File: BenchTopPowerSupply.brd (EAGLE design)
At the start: 160 x 100 mm, 129 parts, among them U10 E2A-T220-25E, U7 STM32F103C8T6, U8 E2A-T220-25E, U9 E2A-T220-25E, X1 5566-24, Y1 8MHZ

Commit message: Fixing schematic issues
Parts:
- added R34: 1M, rcl:R1206
- moved LED1 11.9 mm to (98.7, 35.7)
- moved C19 6.51 mm to (112.4, 26.5), flipped to the top, turned to 225 degrees
- moved R23 2.51 mm to (105.4, 39.1), turned to 0 degrees
- moved C18 1.13 mm to (107.4, 31.9), turned to 225 degrees
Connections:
- new net N$10: C18.2, C19.2
- net BOOT1: now also U7.20; no longer U7.19
- net GND: no longer C18.2, C19.2
- net N$3: now also R34.2
- net N$5: now also R34.1
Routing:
- net N$10: track 0.00 -> 9.96 mm
- net N$3: track 11.2 -> 16.6 mm
- net N$5: track 15.5 -> 17.9 mm
- net N$28: track 7.26 -> 6.16 mm
- net N$27: track 7.04 -> 7.60 mm

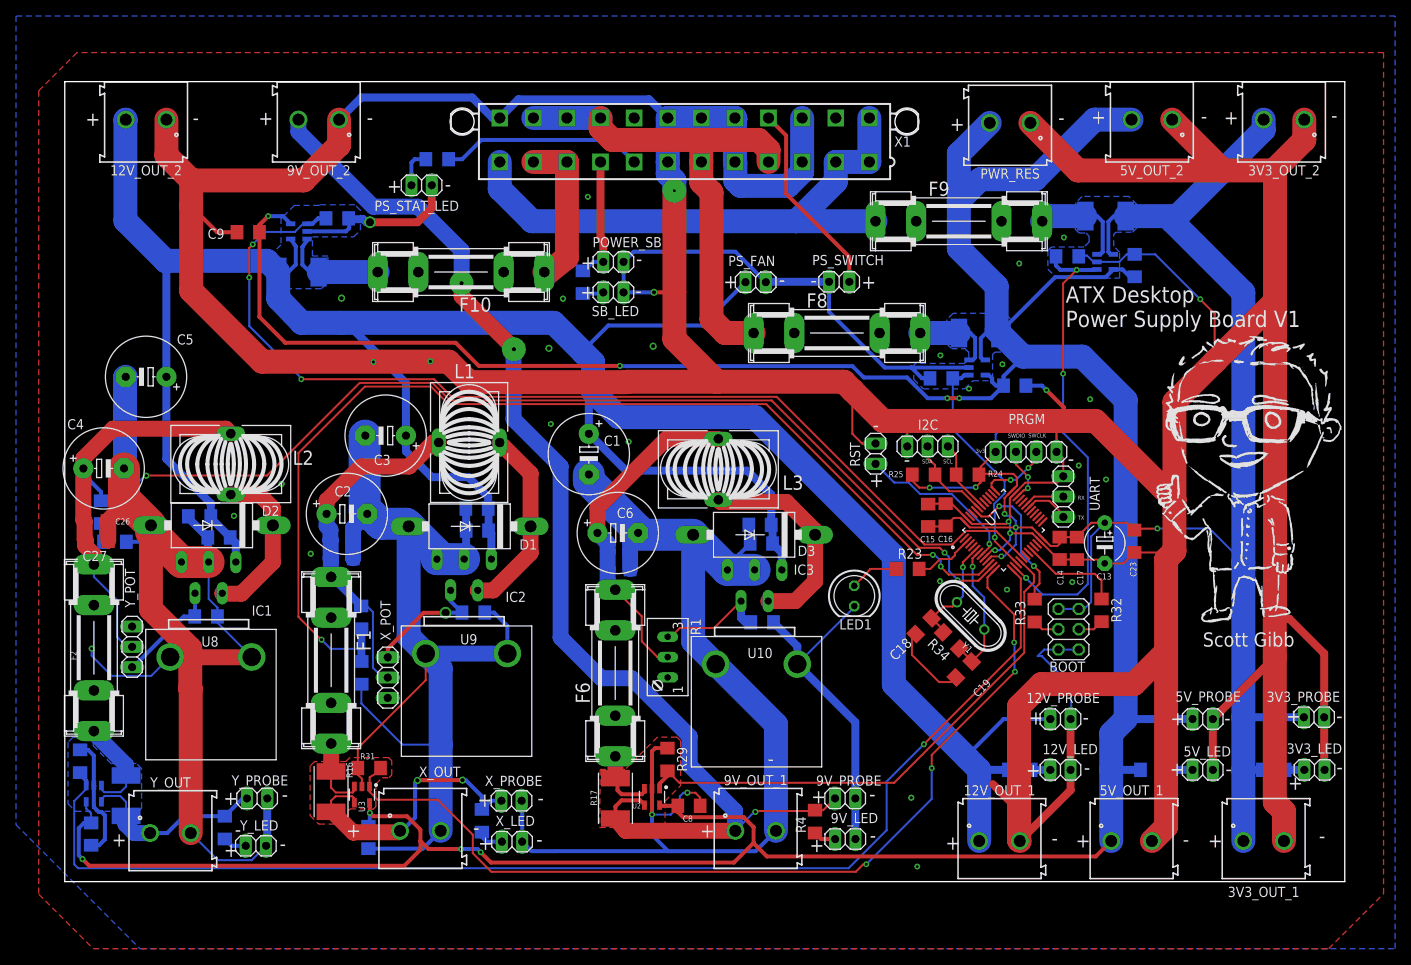
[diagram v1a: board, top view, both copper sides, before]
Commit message: Adding mounting holes to the design and experimenting with JLCPCB SMT assembly
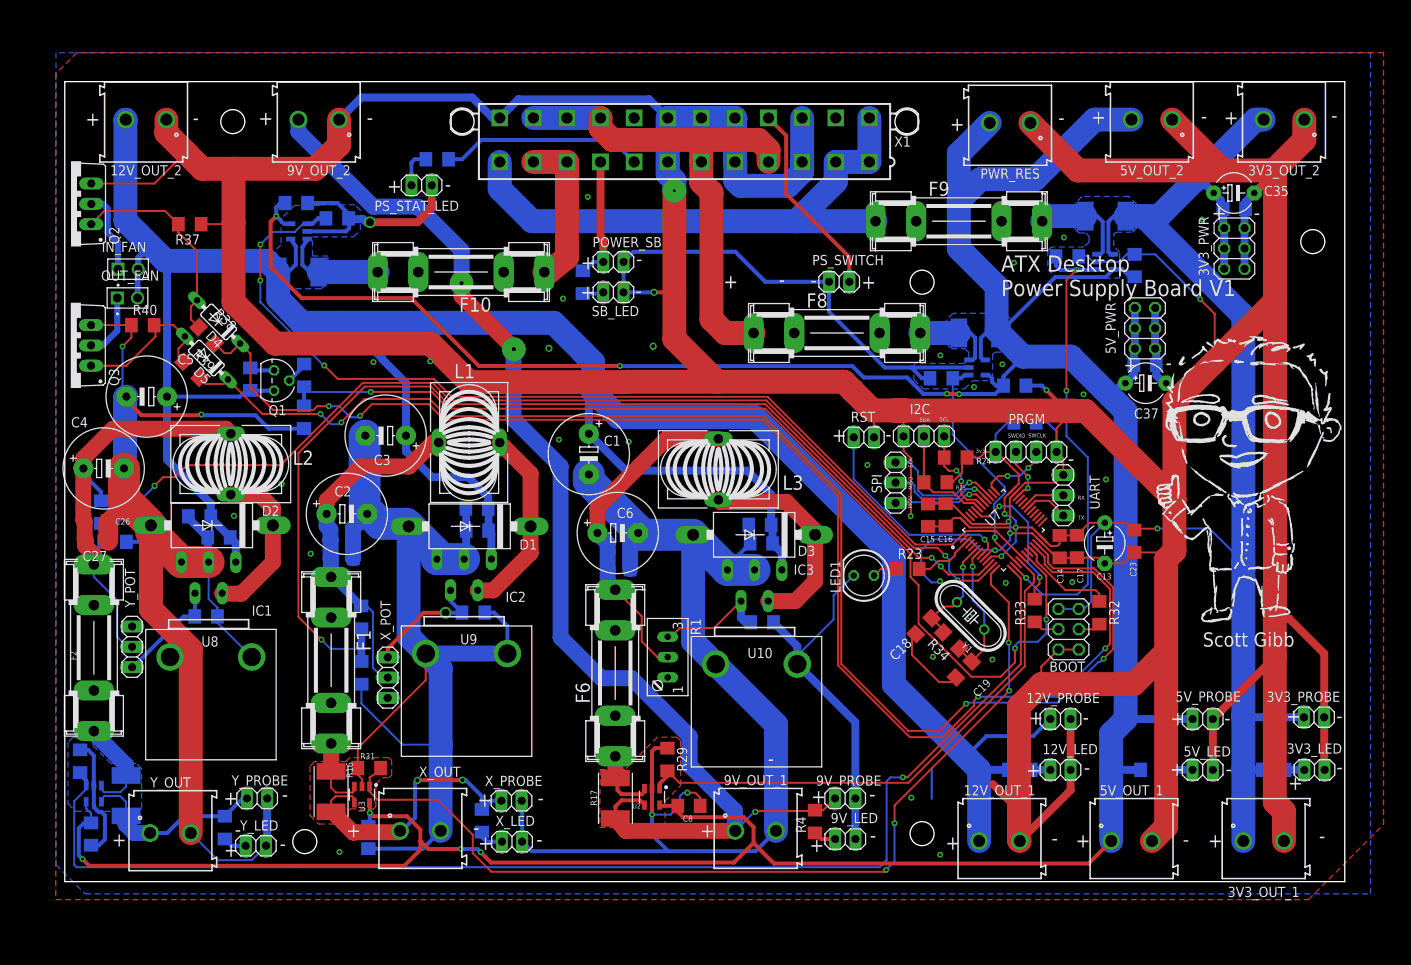
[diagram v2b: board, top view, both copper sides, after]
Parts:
- removed PS_FAN: (no value), pinhead:1X02
- added 3V3_PWR, 5V_PWR: PINHD-2X3, Connector:2X03
- added C34: 100nF, rcl:C1206
- added C35, C37: 100nF, rcl:E5-5
- added C36, C38: 100uF, rcl:C1206
- added D4, D5: 1N4148DO35-7, diode:DO35-7
- added IN_FAN, OUT_FAN: 61300211121, Headers:61300211121
- added Q1: NPN, Transistor:TO92
- added Q2, Q3: IRF510, transistor-power:TO220BV
- added R35, R36, R37, R40: 10k, rcl:R1206
- added R38, R39: 470, rcl:R1206
- added SPI: PINHD-1X3, Connector:1X03
- R1: value (none) -> 100k
- moved C9 7.03 mm to (28.9, 84.8), flipped to the bottom
- moved LED1 2.82 mm to (99.9, 38.3), turned to 180 degrees
- moved R24 2.61 mm to (111.4, 53.0)
- moved RST 2.51 mm to (99.9, 55.5), turned to 180 degrees
- moved C5 2.48 mm to (10.2, 60.6)
- moved R25 1.76 mm to (108.8, 49.9), turned to 0 degrees
- moved I2C 1.34 mm to (107.4, 55.7)
- moved R32 0.41 mm to (129.3, 33.6)
- moved C17 0.24 mm to (126.5, 41.9)
- moved C14 0.20 mm to (124.4, 41.9)
- moved UART 0.17 mm to (124.8, 48.3)
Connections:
- new net IN_FAN_PWM: D4.C, R38.2, U7.21
- new net N$26: Q1.2, R35.2
- new net N$30: D4.A, Q2.G, R37.2, R38.1
- new net N$31: IN_FAN.1, Q2.D
- new net N$32: D5.A, Q3.G, R39.1, R40.2
- new net N$35: OUT_FAN.1, Q3.D
- new net OUT_FAN_PWM: D5.C, R39.2, U7.22
- new net SPI_MISO: SPI.2, U7.40
- new net SPI_MOSI: SPI.3, U7.41
- new net SPI_NSS: U7.38
- new net SPI_SCK: SPI.1, U7.39
- new net TEMP_SENS: R35.1, R36.2, U7.18
- net +12V: now also C34.1, IN_FAN.2, OUT_FAN.2, Q1.1; no longer PS_FAN.1
- net +3V3: now also 3V3_PWR.1, 3V3_PWR.3, 3V3_PWR.5, C35.+, C36.2
- net +5V: now also 5V_PWR.1, 5V_PWR.3, 5V_PWR.5, C37.+, C38.2
- net GND: now also 3V3_PWR.2, 3V3_PWR.4, 3V3_PWR.6, 5V_PWR.2, 5V_PWR.4, 5V_PWR.6, C34.2, C35.-, C36.1, C37.-, C38.1, Q1.3, Q2.S, Q3.S, R36.1, R37.1, R40.1; no longer PS_FAN.2
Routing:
- net IN_FAN_PWM: track 0.00 -> 174.2 mm, vias 0 -> 4
- net OUT_FAN_PWM: track 0.00 -> 172.4 mm, vias 0 -> 4
- net TEMP_SENS: track 0.00 -> 130.2 mm, vias 0 -> 3
- net GND: track 1310.7 -> 1391.4 mm, vias 36 -> 42
- net N$30: track 0.00 -> 26.8 mm
- net N$32: track 0.00 -> 19.8 mm
- net SPI_SCK: track 0.00 -> 16.3 mm, vias 0 -> 1
- net SPI_MISO: track 0.00 -> 13.8 mm, vias 0 -> 1
- net SPI_MOSI: track 0.00 -> 11.9 mm, vias 0 -> 1
- net N$31: track 0.00 -> 10.4 mm
- net +3V3: track 221.2 -> 231.2 mm, vias 6 -> 4
- net +5V: track 461.2 -> 469.4 mm
- net N$35: track 0.00 -> 8.14 mm
- net N$25: track 21.1 -> 27.2 mm
- net X_CURR_OUT: track 118.1 -> 122.9 mm
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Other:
- board text added: "MISO"
- board text added: "MOSI"
- board text added: "SCK"

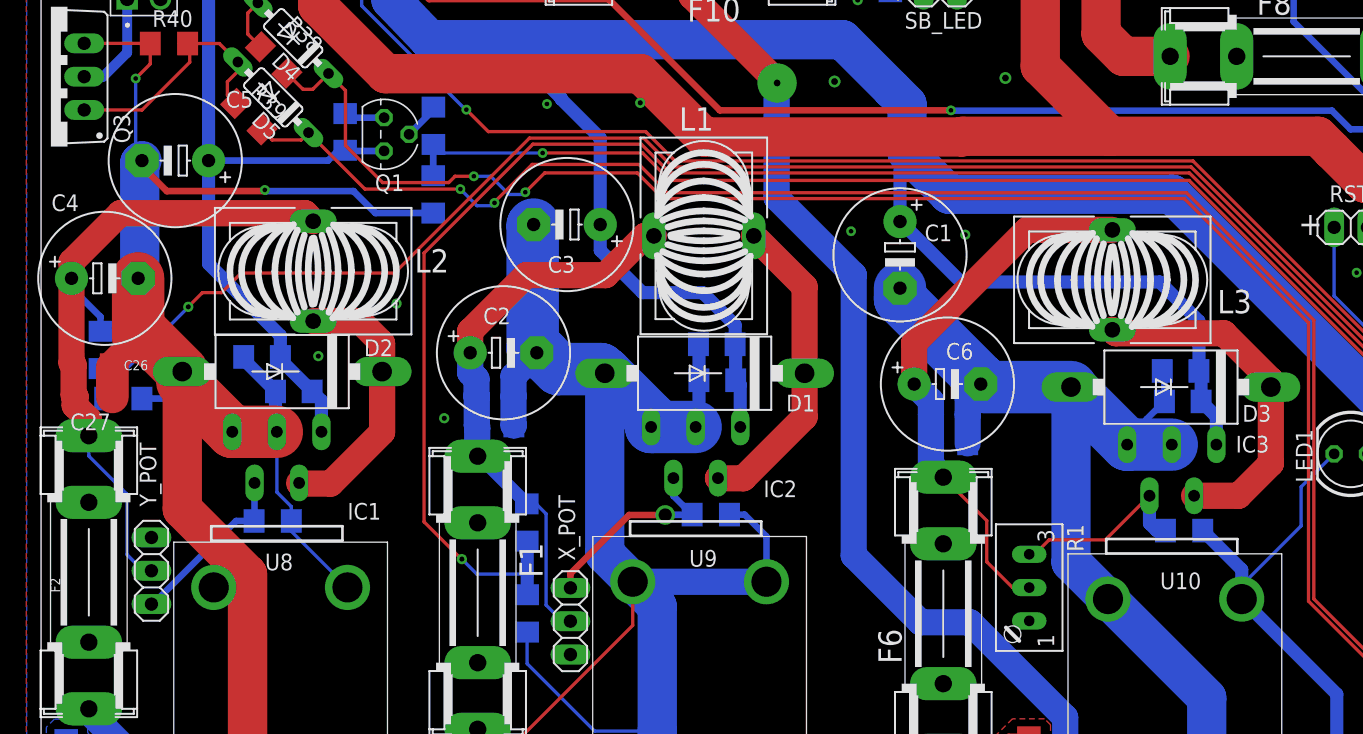
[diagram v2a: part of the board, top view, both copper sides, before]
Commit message: Changing to surface mount inductors, reduce noise on board, hopefully. Will need to redo layout however and figure out how to solder them
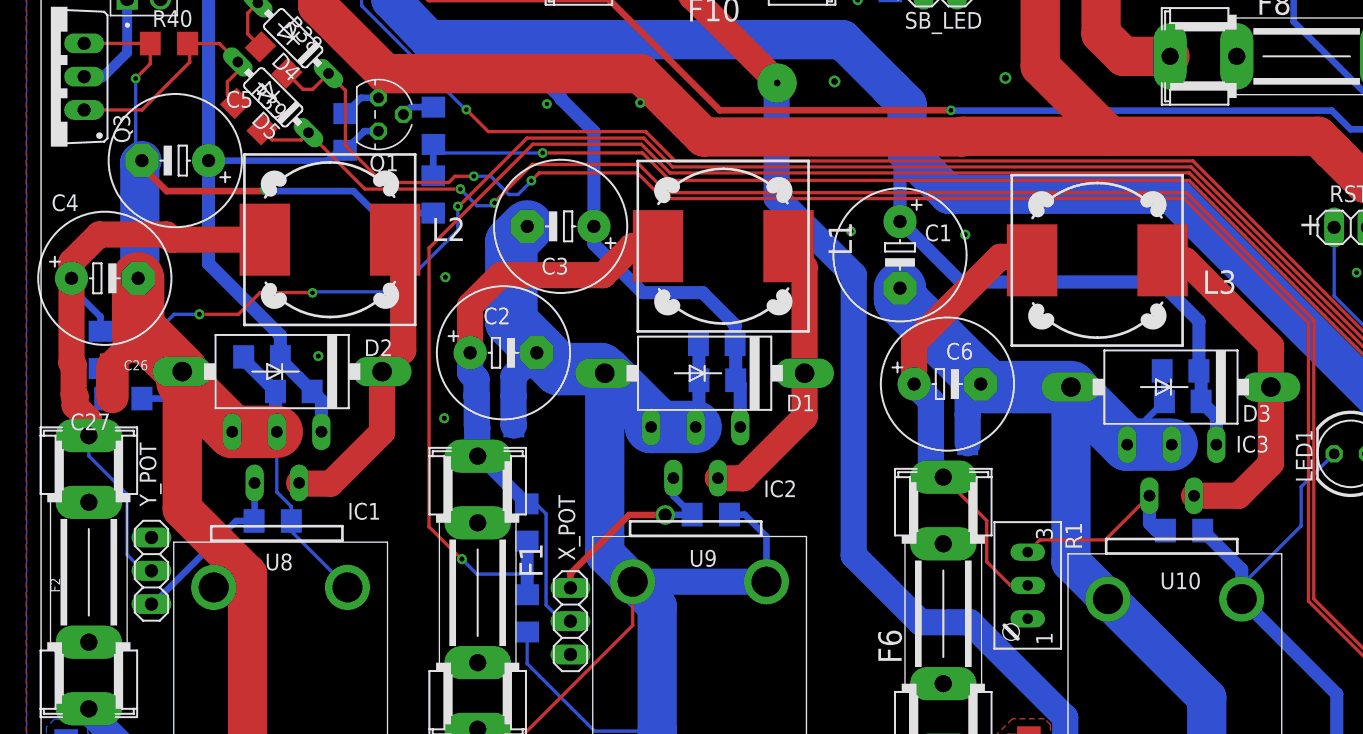
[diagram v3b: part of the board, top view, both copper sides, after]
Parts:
- L1, L2, L3: value A26GFC -> DR125; device inductors:A26GFC -> inductors:DR125
- moved L2 2.72 mm to (22.0, 54.6)
- moved L3 1.87 mm to (80.6, 53.0)
- moved L1 1.68 mm to (52.0, 54.1), turned to 180 degrees
- moved Q1 1.57 mm to (25.7, 64.1)
- moved C3 0.50 mm to (39.6, 55.6)
- moved R1 0.20 mm to (74.0, 28.2)
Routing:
- net N$17: track 41.7 -> 34.7 mm
- net Y_POT_2: track 51.7 -> 47.2 mm
- net N$18: track 20.7 -> 23.6 mm
- net N$4: track 24.0 -> 22.0 mm
- net X_POT_2: track 43.2 -> 44.3 mm
- net Y_VOLT_OUT: track 133.5 -> 134.5 mm, vias 3 -> 5
- net GND: track 1391.4 -> 1392.4 mm

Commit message: updating layout silkskin, one final check then sending away for manufacture
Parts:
- moved L1 0.25 mm to (51.8, 54.2)
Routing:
- net X_POT_2: track 44.3 -> 42.0 mm
- net +12V: track 343.3 -> 341.7 mm
